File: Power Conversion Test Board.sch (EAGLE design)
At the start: 49 parts, among them U1 LM2678, U2 LM2678

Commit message: minor changes
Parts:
- added U$11, U$12, U$6: ET60S, ET60S:ET60S
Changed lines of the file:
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@@
 <grid distance="0.1" unitdist="inch" unit="inch" style="lines" multiple="1" display="no" altdistance="0.01" altunitdist="inch" altunit="inch"/>
 <layers>
-<layer number="1" name="Top" color="4" fill="1" visible="yes" active="no"/>
-<layer number="2" name="Route2" color="16" fill="1" visible="yes" active="no"/>
-<layer number="3" name="Route3" color="17" fill="1" visible="yes" active="no"/>
-<layer number="4" name="Route4" color="18" fill="1" visible="yes" active="no"/>
-<layer number="5" name="Route5" color="19" fill="1" visible="yes" active="no"/>
-<layer number="6" name="Route6" color="25" fill="1" visible="yes" active="no"/>
-<layer number="7" name="Route7" color="26" fill="1" visible="yes" active="no"/>
-<layer number="8" name="Route8" color="27" fill="1" visible="yes" active="no"/>
-<layer number="9" name="Route9" color="28" fill="1" visible="yes" active="no"/>
-<layer number="10" name="Route10" color="29" fill="1" visible="yes" active="no"/>
-<layer number="11" name="Route11" color="30" fill="1" visible="yes" active="no"/>
-<layer number="12" name="Route12" color="20" fill="1" visible="yes" active="no"/>
-<layer number="13" name="Route13" color="21" fill="1" visible="yes" active="no"/>
-<layer number="14" name="Route14" color="22" fill="1" visible="yes" active="no"/>
-<layer number="15" name="Route15" color="23" fill="1" visible="yes" active="no"/>
-<layer number="16" name="Bottom" color="1" fill="1" visible="yes" active="no"/>
-<layer number="17" name="Pads" color="2" fill="1" visible="yes" active="no"/>
-<layer number="18" name="Vias" color="2" fill="1" visible="yes" active="no"/>
-<layer number="19" name="Unrouted" color="6" fill="1" visible="yes" active="no"/>
-<layer number="20" name="Dimension" color="24" fill="1" visible="yes" active="no"/>
-<layer number="21" name="tPlace" color="7" fill="1" visible="yes" active="no"/>
-<layer number="22" name="bPlace" color="7" fill="1" visible="yes" active="no"/>
-<layer number="23" name="tOrigins" color="15" fill="1" visible="yes" active="no"/>
-<layer number="24" name="bOrigins" color="15" fill="1" visible="yes" active="no"/>
-<layer number="25" name="tNames" color="7" fill="1" visible="yes" active="no"/>
-<layer number="26" name="bNames" color="7" fill="1" visible="yes" active="no"/>
-<layer number="27" name="tValues" color="7" fill="1" visible="yes" active="no"/>
-<layer number="28" name="bValues" color="7" fill="1" visible="yes" active="no"/>
+<layer number="1" name="Top" color="4" fill="1" visible="no" active="no"/>
+<layer number="2" name="Route2" color="16" fill="1" visible="no" active="no"/>
+<layer number="3" name="Route3" color="17" fill="1" visible="no" active="no"/>
+<layer number="4" name="Route4" color="18" fill="1" visible="no" active="no"/>
+<layer number="5" name="Route5" color="19" fill="1" visible="no" active="no"/>
+<layer number="6" name="Route6" color="25" fill="1" visible="no" active="no"/>
+<layer number="7" name="Route7" color="26" fill="1" visible="no" active="no"/>
+<layer number="8" name="Route8" color="27" fill="1" visible="no" active="no"/>
+<layer number="9" name="Route9" color="28" fill="1" visible="no" active="no"/>
+<layer number="10" name="Route10" color="29" fill="1" visible="no" active="no"/>
+<layer number="11" name="Route11" color="30" fill="1" visible="no" active="no"/>
+<layer number="12" name="Route12" color="20" fill="1" visible="no" active="no"/>
+<layer number="13" name="Route13" color="21" fill="1" visible="no" active="no"/>
+<layer number="14" name="Route14" color="22" fill="1" visible="no" active="no"/>
+<layer number="15" name="Route15" color="23" fill="1" visible="no" active="no"/>
+<layer number="16" name="Bottom" color="1" fill="1" visible="no" active="no"/>
+<layer number="17" name="Pads" color="2" fill="1" visible="no" active="no"/>
+<layer number="18" name="Vias" color="2" fill="1" visible="no" active="no"/>
+<layer number="19" name="Unrouted" color="6" fill="1" visible="no" active="no"/>
+<layer number="20" name="Dimension" color="24" fill="1" visible="no" active="no"/>
+<layer number="21" name="tPlace" color="7" fill="1" visible="no" active="no"/>
+<layer number="22" name="bPlace" color="7" fill="1" visible="no" active="no"/>
+<layer number="23" name="tOrigins" color="15" fill="1" visible="no" active="no"/>
+<layer number="24" name="bOrigins" color="15" fill="1" visible="no" active="no"/>
+<layer number="25" name="tNames" color="7" fill="1" visible="no" active="no"/>
+<layer number="26" name="bNames" color="7" fill="1" visible="no" active="no"/>
+<layer number="27" name="tValues" color="7" fill="1" visible="no" active="no"/>
+<layer number="28" name="bValues" color="7" fill="1" visible="no" active="no"/>
 <layer number="29" name="tStop" color="7" fill="3" visible="no" active="no"/>
 <layer number="30" name="bStop" color="7" fill="6" visible="no" active="no"/>
@@
 <layer number="35" name="tGlue" color="7" fill="4" visible="no" active="no"/>
 <layer number="36" name="bGlue" color="7" fill="5" visible="no" active="no"/>
-<layer number="37" name="tTest" color="7" fill="1" visible="yes" active="no"/>
-<layer number="38" name="bTest" color="7" fill="1" visible="yes" active="no"/>
+<layer number="37" name="tTest" color="7" fill="1" visible="no" active="no"/>
+<layer number="38" name="bTest" color="7" fill="1" visible="no" active="no"/>
 <layer number="39" name="tKeepout" color="4" fill="11" visible="no" active="no"/>
 <layer number="40" name="bKeepout" color="1" fill="11" visible="no" active="no"/>
@@
 <layer number="44" name="Drills" color="7" fill="1" visible="no" active="no"/>
 <layer number="45" name="Holes" color="7" fill="1" visible="no" active="no"/>
-<layer number="46" name="Milling" color="3" fill="1" visible="yes" active="no"/>
-<layer number="47" name="Measures" color="7" fill="1" visible="yes" active="no"/>
-<layer number="48" name="Document" color="7" fill="1" visible="yes" active="no"/>
-<layer number="49" name="Reference" color="7" fill="1" visible="yes" active="no"/>
-<layer number="50" name="dxf" color="7" fill="1" visible="yes" active="no"/>
-<layer number="51" name="tDocu" color="7" fill="1" visible="yes" active="no"/>
-<layer number="52" name="bDocu" color="7" fill="1" visible="yes" active="no"/>
-<layer number="53" name="tGND_GNDA" color="7" fill="9" visible="yes" active="no"/>
-<layer number="54" name="bGND_GNDA" color="1" fill="9" visible="yes" active="no"/>
-<layer number="56" name="wert" color="7" fill="1" visible="yes" active="no"/>
-<layer number="57" name="tCAD" color="7" fill="1" visible="yes" active="no"/>
-<layer number="59" name="tCarbon" color="7" fill="1" visible="yes" active="no"/>
-<layer number="60" name="bCarbon" color="7" fill="1" visible="yes" active="no"/>
+<layer number="46" name="Milling" color="3" fill="1" visible="no" active="no"/>
+<layer number="47" name="Measures" color="7" fill="1" visible="no" active="no"/>
+<layer number="48" name="Document" color="7" fill="1" visible="no" active="no"/>
+<layer number="49" name="Reference" color="7" fill="1" visible="no" active="no"/>
+<layer number="50" name="dxf" color="7" fill="1" visible="no" active="no"/>
+<layer number="51" name="tDocu" color="7" fill="1" visible="no" active="no"/>
+<layer number="52" name="bDocu" color="7" fill="1" visible="no" active="no"/>
+<layer number="53" name="tGND_GNDA" color="7" fill="9" visible="no" active="no"/>
+<layer number="54" name="bGND_GNDA" color="1" fill="9" visible="no" active="no"/>
+<layer number="56" name="wert" color="7" fill="1" visible="no" active="no"/>
+<layer number="57" name="tCAD" color="7" fill="1" visible="no" active="no"/>
+<layer number="59" name="tCarbon" color="7" fill="1" visible="no" active="no"/>
+<layer number="60" name="bCarbon" color="7" fill="1" visible="no" active="no"/>
 <layer number="88" name="SimResults" color="9" fill="1" visible="yes" active="yes"/>
 <layer number="89" name="SimProbes" color="9" fill="1" visible="yes" active="yes"/>
@@
 </part>
 <part name="U$2" library="PDB_PCB_connectors" deviceset="PDB_PCB_CONNEC" device=""/>
+<part name="U$6" library="ET60S" deviceset="ET60S" device=""/>
+<part name="U$11" library="ET60S" deviceset="ET60S" device=""/>
+<part name="U$12" library="ET60S" deviceset="ET60S" device=""/>
 </parts>
 <sheets>
@@
 <instance part="R7" gate="G$1" x="203.2" y="106.68"/>
 <instance part="U$2" gate="G$1" x="231.14" y="-101.6"/>
+<instance part="U$6" gate="G$2" x="45.72" y="-60.96"/>
+<instance part="U$11" gate="G$2" x="88.9" y="-60.96"/>
+<instance part="U$12" gate="G$2" x="132.08" y="-60.96"/>
 </instances>
 <busses>

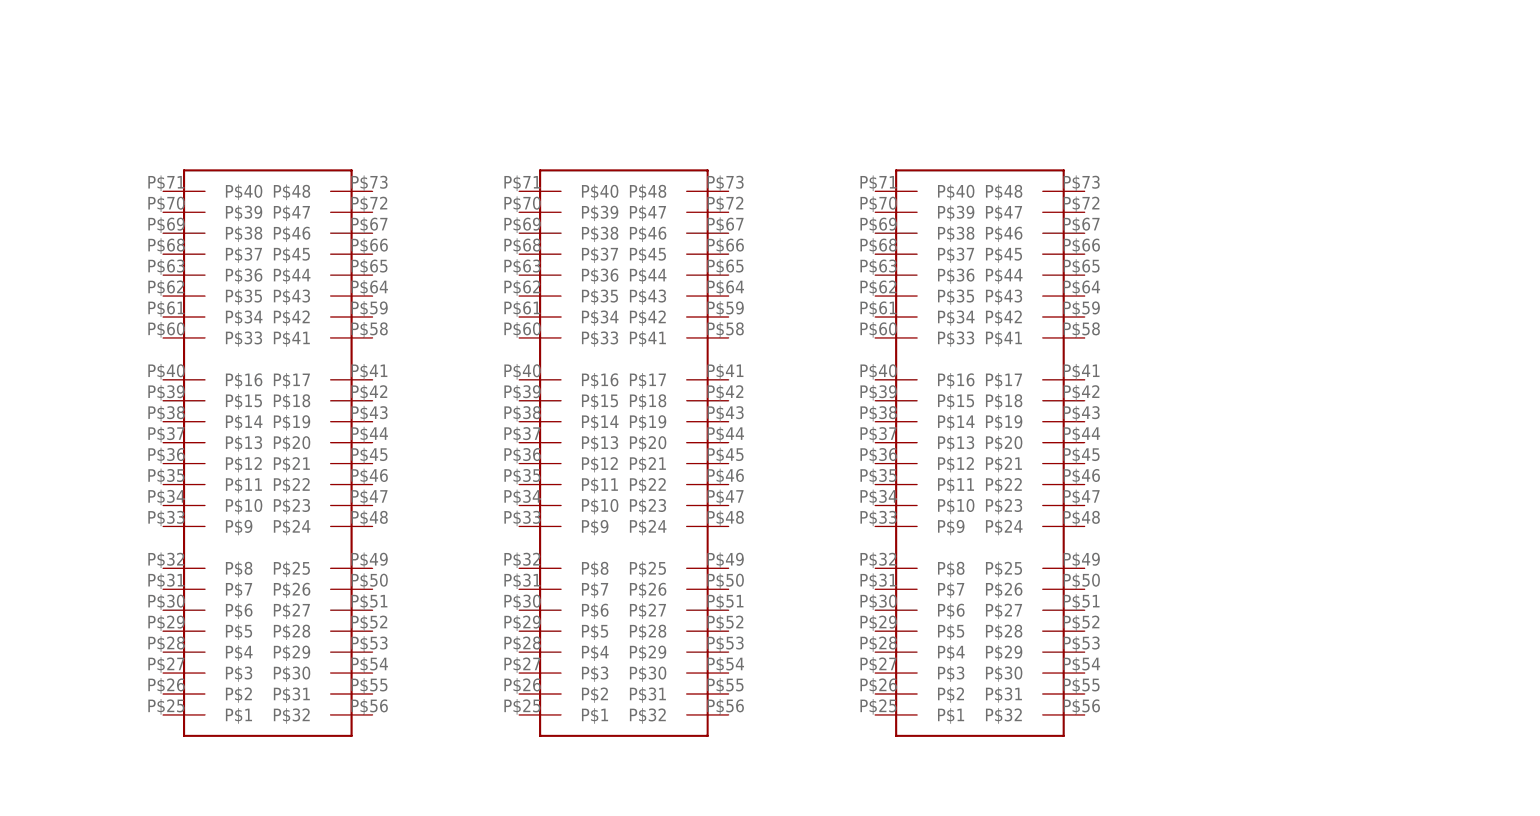
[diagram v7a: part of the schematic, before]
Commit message: Netted connectors
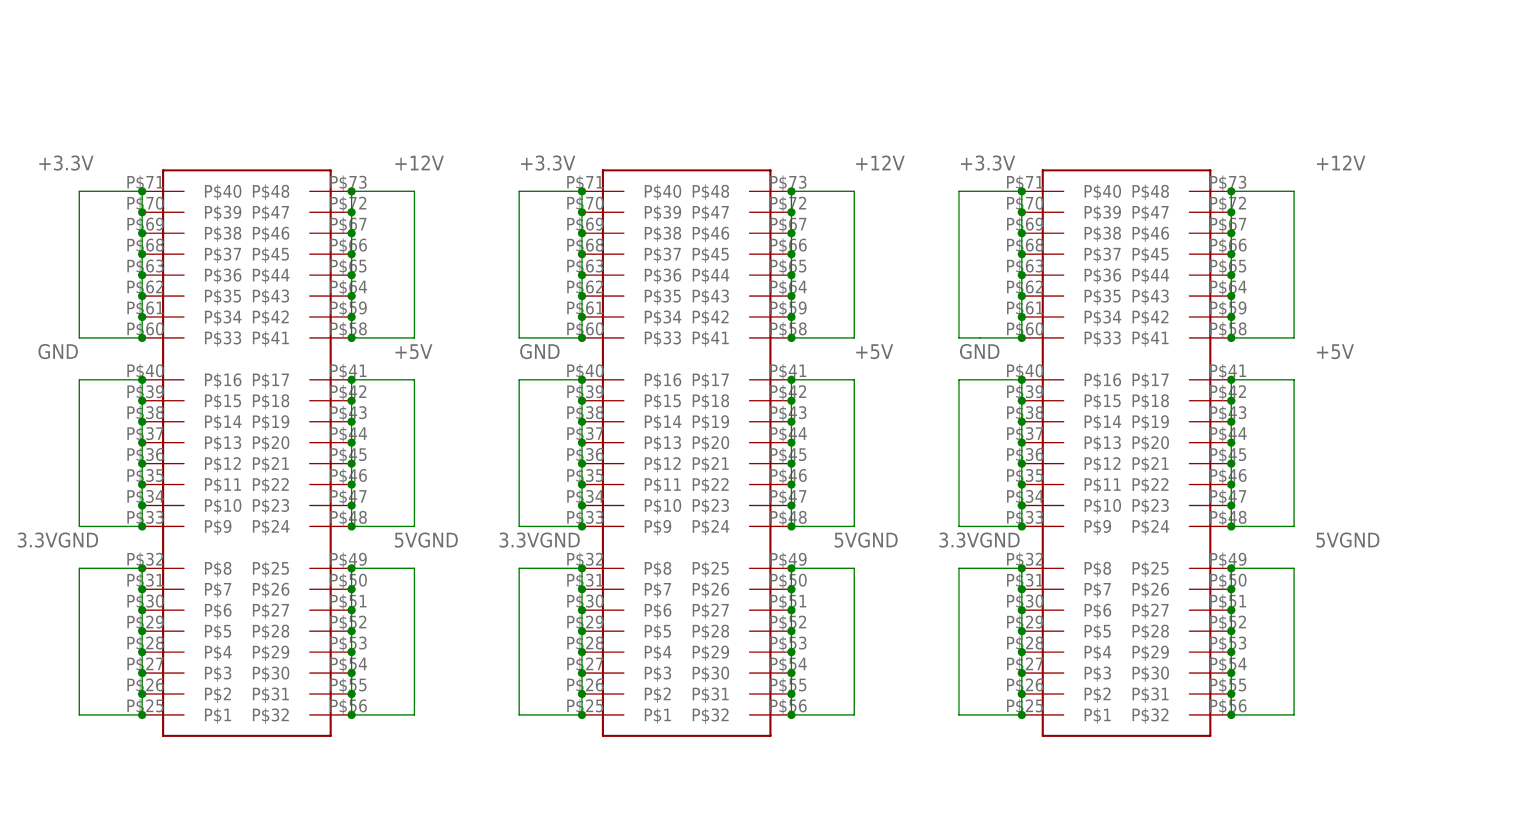
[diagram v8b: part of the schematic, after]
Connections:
- net +12V: now also U$11.P$41, U$11.P$42, U$11.P$43, U$11.P$44, U$11.P$45, U$11.P$46, U$11.P$47, U$11.P$48, U$12.P$41, U$12.P$42, U$12.P$43, U$12.P$44, U$12.P$45, U$12.P$46, U$12.P$47, U$12.P$48, U$6.P$41, U$6.P$42, U$6.P$43, U$6.P$44, U$6.P$45, U$6.P$46, U$6.P$47, U$6.P$48
- net +3.3V: now also U$11.P$33, U$11.P$34, U$11.P$35, U$11.P$36, U$11.P$37, U$11.P$38, U$11.P$39, U$11.P$40, U$12.P$33, U$12.P$34, U$12.P$35, U$12.P$36, U$12.P$37, U$12.P$38, U$12.P$39, U$12.P$40, U$6.P$33, U$6.P$34, U$6.P$35, U$6.P$36, U$6.P$37, U$6.P$38, U$6.P$39, U$6.P$40
- net +5V: now also U$11.P$17, U$11.P$18, U$11.P$19, U$11.P$20, U$11.P$21, U$11.P$22, U$11.P$23, U$11.P$24, U$12.P$17, U$12.P$18, U$12.P$19, U$12.P$20, U$12.P$21, U$12.P$22, U$12.P$23, U$12.P$24, U$6.P$17, U$6.P$18, U$6.P$19, U$6.P$20, U$6.P$21, U$6.P$22, U$6.P$23, U$6.P$24
- net 3.3VGND: now also U$11.P$1, U$11.P$2, U$11.P$3, U$11.P$4, U$11.P$5, U$11.P$6, U$11.P$7, U$11.P$8, U$12.P$1, U$12.P$2, U$12.P$3, U$12.P$4, U$12.P$5, U$12.P$6, U$12.P$7, U$12.P$8, U$6.P$1, U$6.P$2, U$6.P$3, U$6.P$4, U$6.P$5, U$6.P$6, U$6.P$7, U$6.P$8
- net 5VGND: now also U$11.P$25, U$11.P$26, U$11.P$27, U$11.P$28, U$11.P$29, U$11.P$30, U$11.P$31, U$11.P$32, U$12.P$25, U$12.P$26, U$12.P$27, U$12.P$28, U$12.P$29, U$12.P$30, U$12.P$31, U$12.P$32, U$6.P$25, U$6.P$26, U$6.P$27, U$6.P$28, U$6.P$29, U$6.P$30, U$6.P$31, U$6.P$32
- net GND: now also U$11.P$10, U$11.P$11, U$11.P$12, U$11.P$13, U$11.P$14, U$11.P$15, U$11.P$16, U$11.P$9, U$12.P$10, U$12.P$11, U$12.P$12, U$12.P$13, U$12.P$14, U$12.P$15, U$12.P$16, U$12.P$9, U$6.P$10, U$6.P$11, U$6.P$12, U$6.P$13, U$6.P$14, U$6.P$15, U$6.P$16, U$6.P$9
